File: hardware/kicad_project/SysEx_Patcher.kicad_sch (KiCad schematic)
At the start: 83 parts, among them J1 MIDI IN, J10 JACK 6.35 pot deporte, J2 MIDI OUT, J3 DC +5V, J4 BAT/PWR, J5 OLED SSD1306, J6 MEGA ANALOG A0-A15, J7 MEGA DIGITAL, J8 MEGA POWER, J9 MUX SPARE ch2-15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

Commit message: hardware: re-sync schematic to the shield PCB
Regenerated the schematic from the shield's exact component list (Mega header
strips JMA/JMD, custom MIDI DIN-5 + Neutrik jack symbols/footprints, CD74HC4067
mux, RC filters). Refs/nets/footprints now match the .kicad_pcb (86 common refs,
0 ERC errors), so 'Update PCB from Schematic' is consistent again.
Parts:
- removed D2: 1N4004, Diode_THT:D_DO-41_SOD81_P10.16mm_Horizontal, symbol Device:D
- removed J6: MEGA ANALOG A0-A15, Connector_PinHeader_2.54mm:PinHeader_1x16_P2.54mm_Vertical, symbol Connector_Generic:Conn_01x16
- removed J7: MEGA DIGITAL, Connector_PinHeader_2.54mm:PinHeader_1x16_P2.54mm_Vertical, symbol Connector_Generic:Conn_01x16
- removed J8: MEGA POWER, Connector_PinHeader_2.54mm:PinHeader_1x03_P2.54mm_Vertical, symbol Connector_Generic:Conn_01x03
- removed J9: MUX SPARE ch2-15, Connector_PinHeader_2.54mm:PinHeader_1x14_P2.54mm_Vertical, symbol Connector_Generic:Conn_01x14
- added D2D: 1N4004, Diode_THT:D_DO-41_SOD81_P10.16mm_Horizontal, symbol Device:D
- added JMA1, JMA2, JMA3: MEGA, Connector_PinHeader_2.54mm:PinHeader_1x08_P2.54mm_Vertical, symbol Connector_Generic:Conn_01x08
- added JMD1: MEGA, Connector_PinHeader_2.54mm:PinHeader_1x10_P2.54mm_Vertical, symbol Connector_Generic:Conn_01x10
- added JMD2: MEGA, Connector_PinHeader_2.54mm:PinHeader_1x03_P2.54mm_Vertical, symbol Connector_Generic:Conn_01x03
- added JMD3, JMD4: MEGA, Connector_PinHeader_2.54mm:PinHeader_1x02_P2.54mm_Vertical, symbol Connector_Generic:Conn_01x02
- J1: value MIDI IN -> MIDI_IN; footprint Connector_Audio:Jack_DIN_5pin -> SysEx_Patcher:MIDI_DIN5_180deg
- J10: value JACK 6.35 pot deporte -> JACK6.35; footprint Connector_Audio:Jack_6.35mm_Switched -> Connector_Audio:Jack_6.35mm_Neutrik_NJ3FD-V_Vertical
- J2: value MIDI OUT -> MIDI_OUT; footprint Connector_Audio:Jack_DIN_5pin -> SysEx_Patcher:MIDI_DIN5_180deg
- J3: value DC +5V -> DC_5V
- J4: value BAT/PWR -> BAT_PWR
- J5: value OLED SSD1306 -> OLED
- SW2: value PAGE/SHIFT -> SW
- SW3: value CALLBACK/START -> SW
- SW4: value RNDMZ!/PANIC -> SW
- SW5: value MODE -> SW
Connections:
- net +5V: now also D2D.1 (K), JMA1.5 (Pin_5)
- net A0: now also JMA2.1 (Pin_1)
- net A1: now also JMA2.2 (Pin_2)
- net A10: now also JMA3.3 (Pin_3)
- net A11: now also JMA3.4 (Pin_4)
- net A12: now also JMA3.5 (Pin_5)
- net A13: now also JMA3.6 (Pin_6)
- net A14: now also JMA3.7 (Pin_7)
- net A15: now also JMA3.8 (Pin_8)
- net A2: now also JMA2.3 (Pin_3)
- net A3: now also JMA2.4 (Pin_4)
- net A4: now also JMA2.5 (Pin_5)
- net A5: now also JMA2.6 (Pin_6)
- net A6: now also JMA2.7 (Pin_7)
- net A7: now also JMA2.8 (Pin_8)
- net A8: now also JMA3.1 (Pin_1)
- net A9: now also JMA3.2 (Pin_2)
- net D0_RX: now also JMD3.2 (Pin_2)
- net D10: now also JMD2.1 (Pin_1)
- net D11: now also JMD2.2 (Pin_2)
- net D12: now also JMD2.3 (Pin_3)
- net D1_TX: now also JMD3.1 (Pin_1)
- net D2: now also JMD1.1 (Pin_1)
- net D20_SDA: now also JMD4.1 (Pin_1)
- net D21_SCL: now also JMD4.2 (Pin_2)
- net D3: now also JMD1.2 (Pin_2)
- net D4: now also JMD1.3 (Pin_3)
- net D5: now also JMD1.6 (Pin_6)
- net D6: now also JMD1.7 (Pin_7)
- net D7: now also JMD1.8 (Pin_8)
- net D8: now also JMD1.9 (Pin_9)
- net D9: now also JMD1.10 (Pin_10)
- net GND: now also JMA1.6 (Pin_6), JMA1.7 (Pin_7), JMD1.4 (Pin_4)
- net VIN_RAW: now also D2D.2 (A), JMA1.8 (Pin_8)
- net D22 renamed D13
- net D13: now also JMD1.5 (Pin_5)
- no-connect marks 7 -> 11

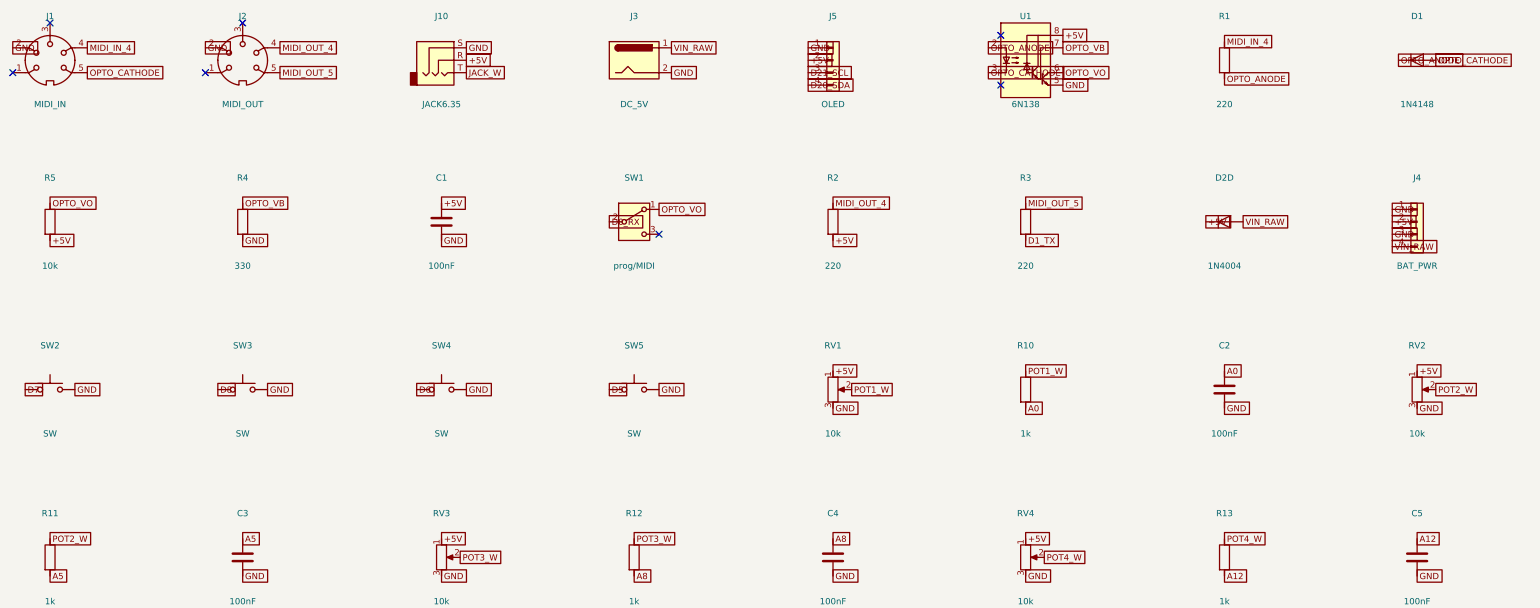
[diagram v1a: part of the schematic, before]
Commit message: hardware: fix connector orientations + horizontal jack, reroute clean
- MIDI DIN-5 (J1/J2): rebuild footprint to match original PCB orientation
  (mount holes at top, signal arc below, data pins 4/5 lowest) — was upside down
- 6.35mm jack (J10): switch to Neutrik NRJ6HF-1 horizontal, nose toward the top
  edge so the cable plugs in horizontally from the top (was vertical NJ3FD-V)
- DC barrel (J3): rotate 270deg so the opening faces the top edge like the
  other inputs (was facing left)
- OLED (J5): plain 1x4 header, no pin-name silkscreen
- move 4067 mux + jack RC filter into the gap between the two Mega header rows
  to declutter the dense analog header row (fixes autorouter A15/D10 shorts)
- full reroute: 0 unconnected, DRC clean; regenerate fab Gerbers + previews
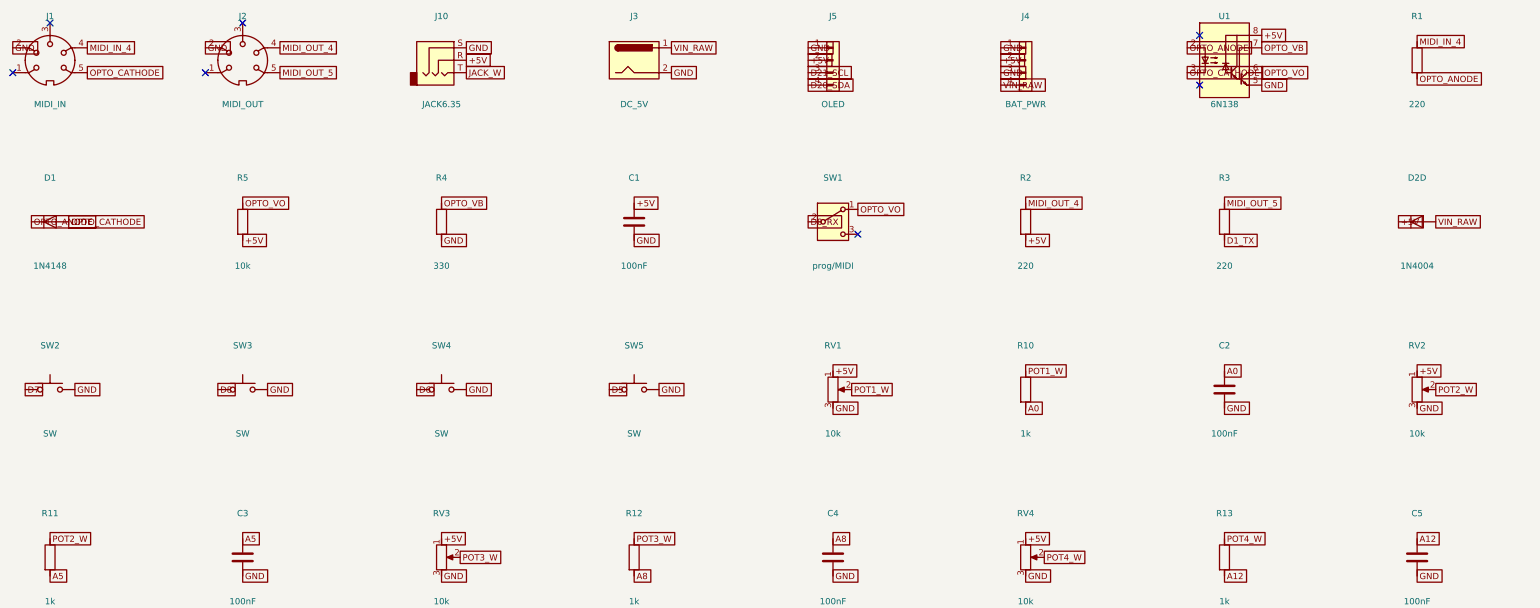
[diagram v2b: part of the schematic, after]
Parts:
- J10: footprint Connector_Audio:Jack_6.35mm_Neutrik_NJ3FD-V_Vertical -> Connector_Audio:Jack_6.35mm_Neutrik_NRJ6HF-1_Horizontal

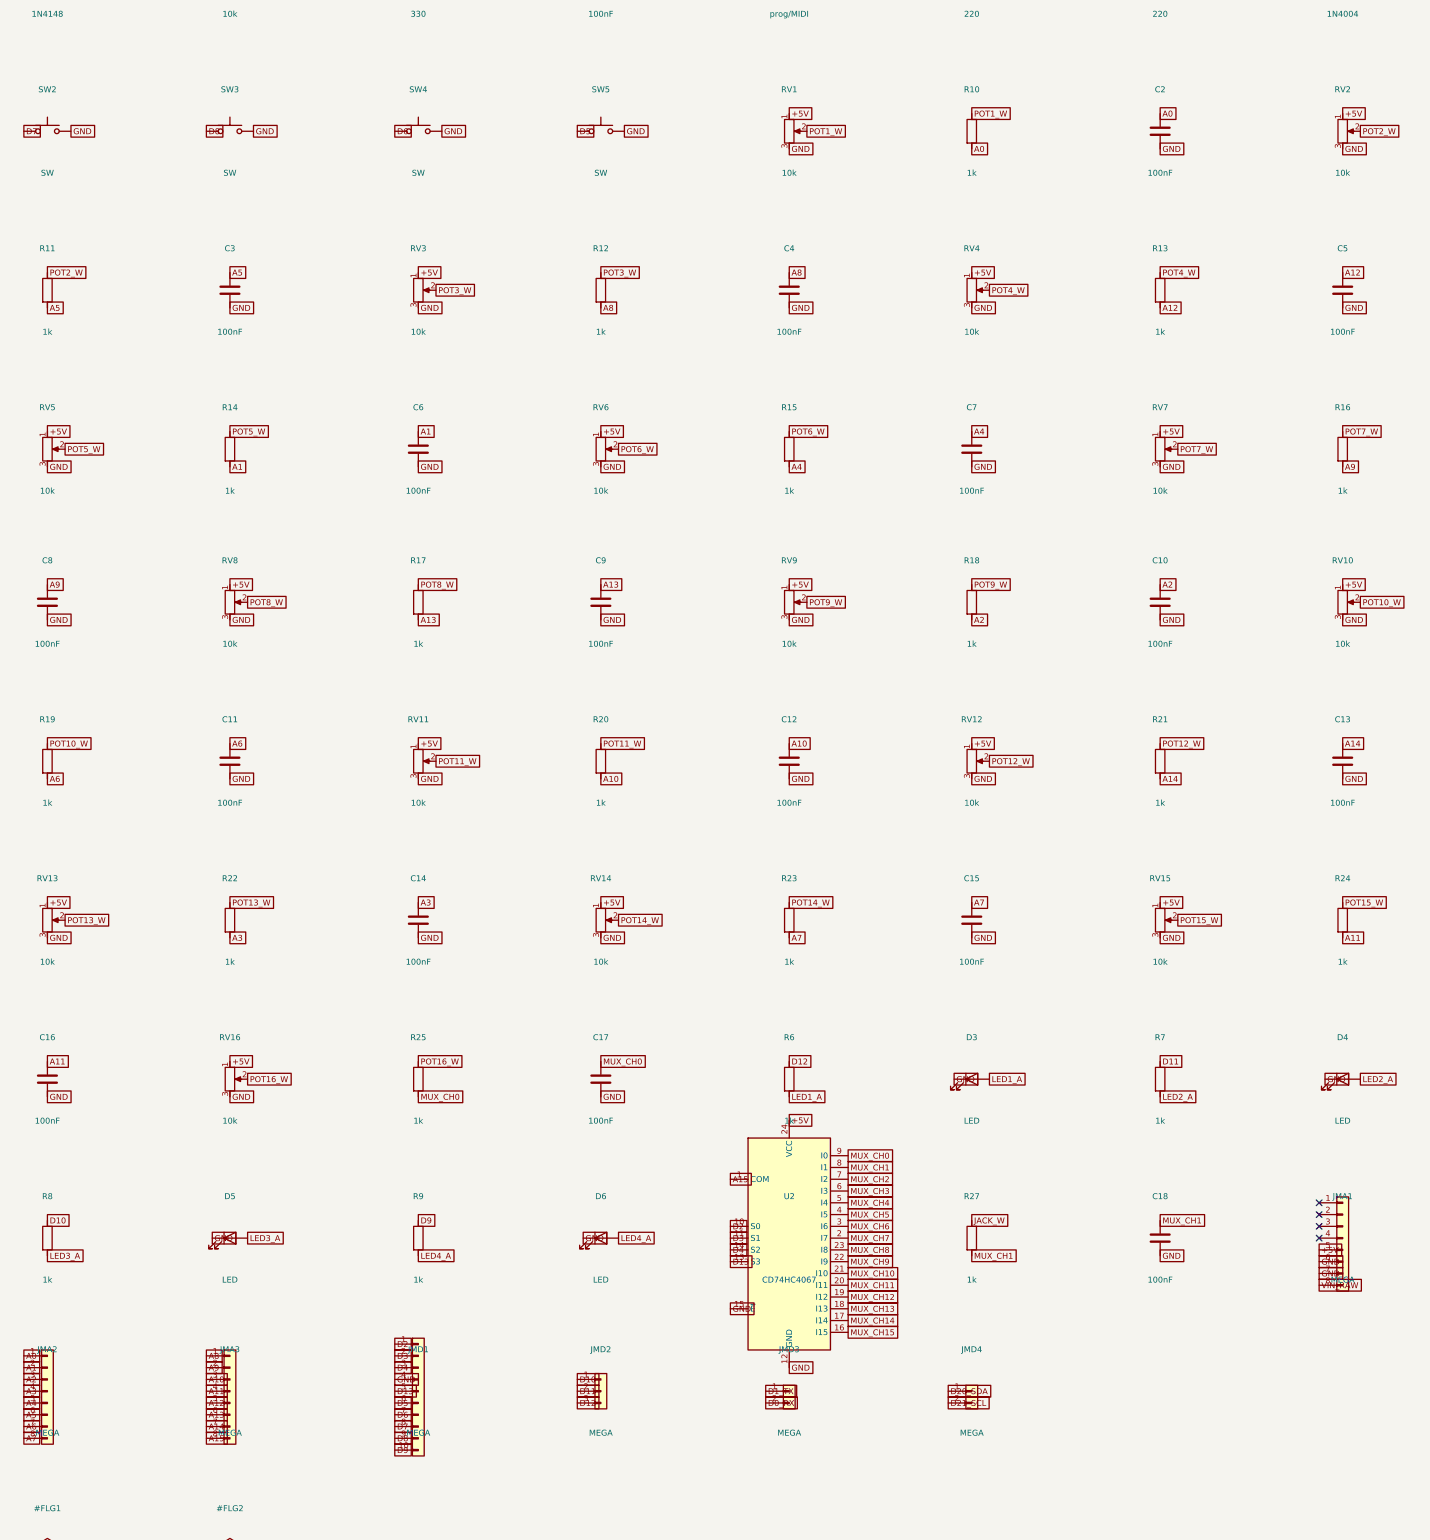
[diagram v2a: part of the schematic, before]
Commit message: hardware: add polarised 100uF electrolytic (C19) on the +5V rail
- C19 = CP_Radial D6.3mm electrolytic across +5V/GND (pad1 + -> +5V, pad2 - -> GND)
  with silkscreen polarity '+' marker and 100uF value label
- schematic: C19 uses Device:C_Polarized symbol
- reroute 0 unconnected, DRC clean, ERC clean (only the 14 intentional spare
  mux-channel warnings); fab Gerbers, schematic PDF, previews + BOM updated
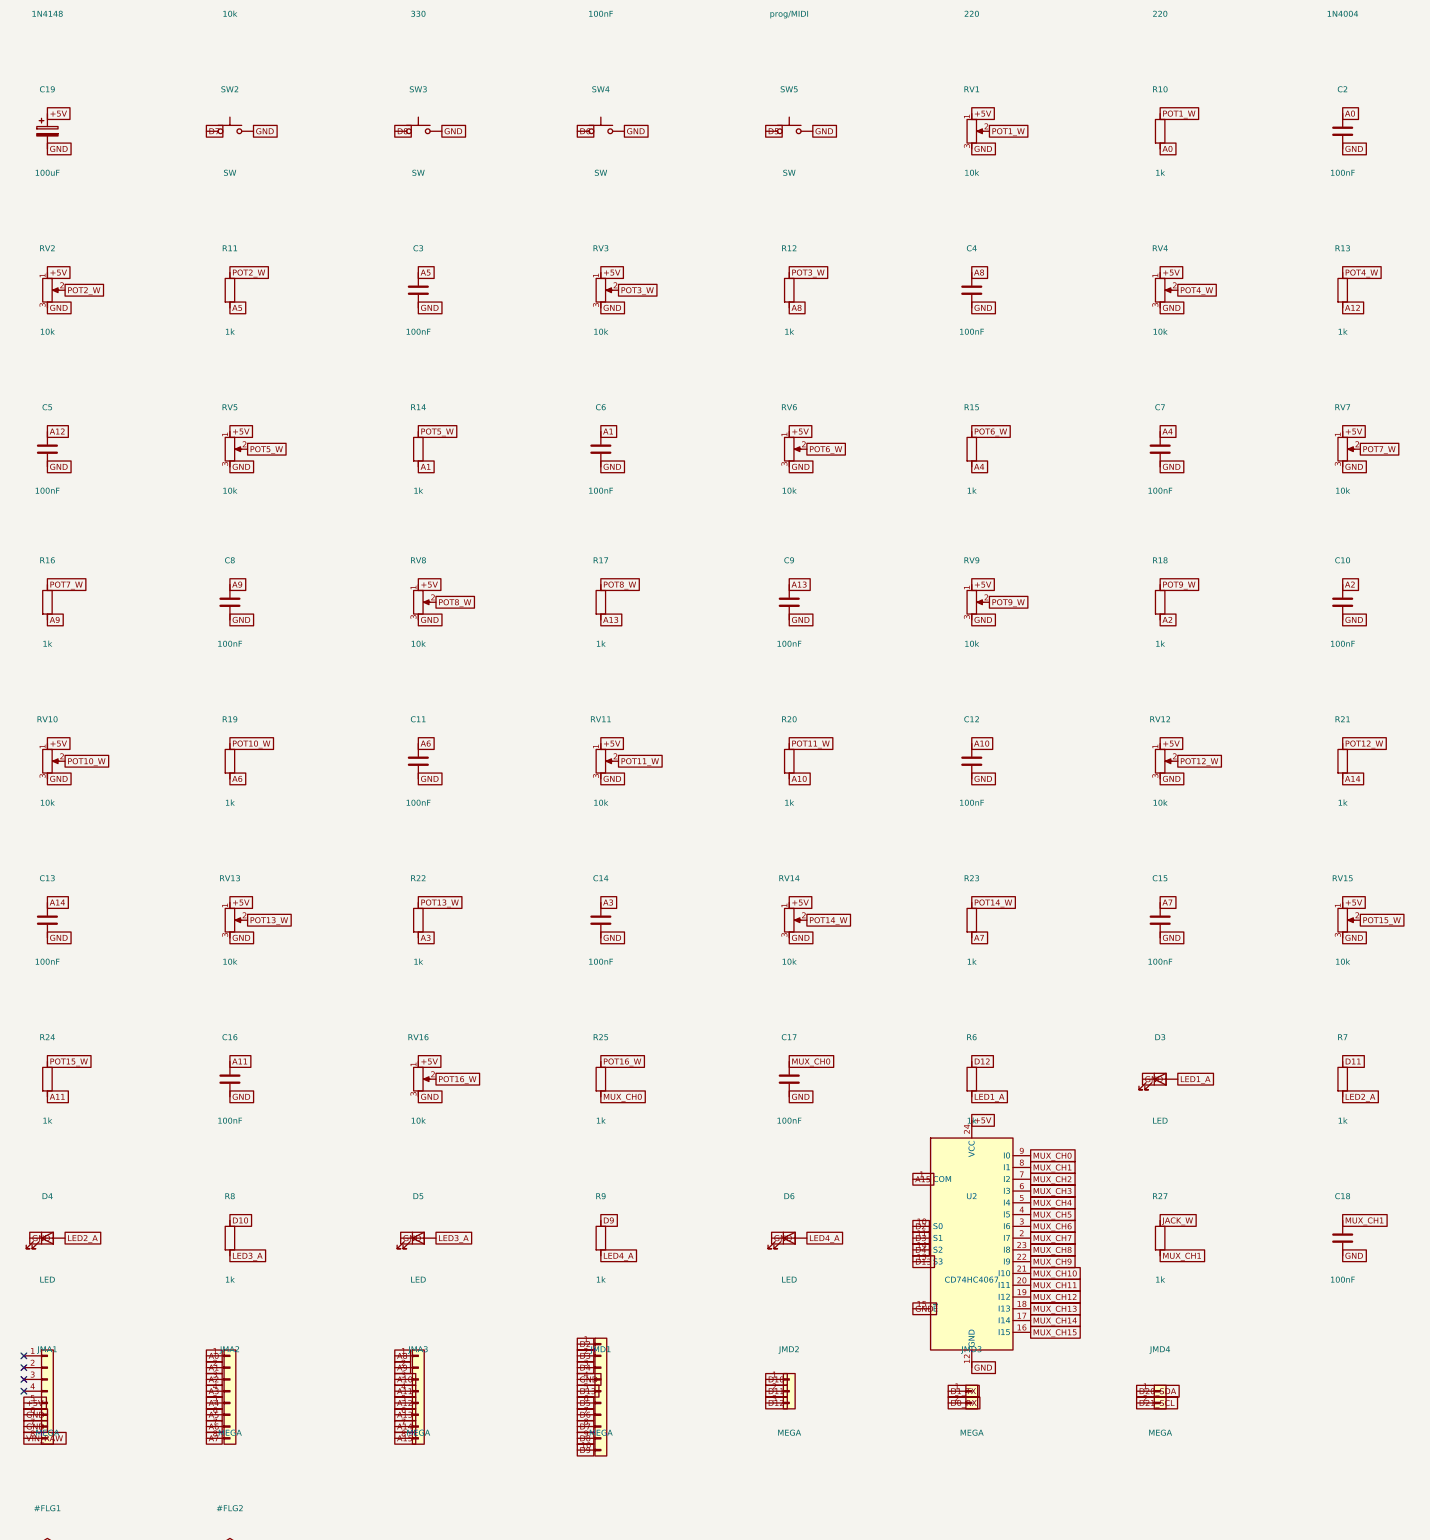
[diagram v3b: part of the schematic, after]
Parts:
- added C19: 100uF, Capacitor_THT:CP_Radial_D6.3mm_P2.50mm, symbol Device:C_Polarized
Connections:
- net +5V: now also C19.1
- net GND: now also C19.2

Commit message: hardware: clean, fully-wired schematic (organized by functional block)
Replace the flat label-on-pin schematic with a readable single-sheet design:
- components grouped into titled blocks (power, MIDI IN/OUT, jack, buttons,
  LEDs, OLED, mux, Mega headers, 16 pot RC filters)
- power symbols (+5V/GND) and net labels on wired stubs
- each of the 16 pots drawn as a wired RC filter cell (pot -> 1k series ->
  100nF to GND, wiper + ADC node labelled)
- ERC clean except the 14 intentional spare 4067 mux-channel labels
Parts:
- removed J10: JACK6.35, Connector_Audio:Jack_6.35mm_Neutrik_NRJ6HF-1_Horizontal, symbol Connector_Audio:AudioJack3
- added J10: JACK6.35, Connector_Audio:Jack_6.35mm_Neutrik_NRJ6HF-1_Horizontal, symbol Connector_Generic:Conn_01x04
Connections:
- net +5V: now also J10.2 (Pin_2)
- net GND: now also J10.3 (Pin_3), J10.4 (Pin_4)
- net JACK_W: now also J10.1 (Pin_1)
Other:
- note added: "ALIMENTATION"
- note added: "ARDUINO MEGA 2560 (embases shield)"
- note added: "BOUTONS"
- note added: "JACK 6.35 (pot deporte)"
- note added: "LEDS"
- note added: "MIDI IN"
- note added: "MIDI OUT"
- note added: "MUX CD74HC4067"
- note added: "OLED I2C"
- note added: "POTENTIOMETRES 16x (filtre RC: 1k serie + 100nF)"
